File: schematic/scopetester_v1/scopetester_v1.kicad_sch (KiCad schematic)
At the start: 42 parts, among them J1 CON_PWR, J2 Conn_01x04, J3 AVR_ISP, SW1 SW_Push, U1 ATmega8A-P, Y1 12MHz

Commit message: Multiple fixes to PCB layout (not final)
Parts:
- added JP1: Jumper_2_Bridged, Resistor_THT:R_Axial_DIN0207_L6.3mm_D2.5mm_P7.62mm_Horizontal, symbol Jumper:Jumper_2_Bridged
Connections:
- net GND: now also JP1.1 (A), JP1.2 (B)
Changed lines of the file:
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@@
-    (stroke (width 0) (type default) (color 0 0 0 0))
-  )
-  (wire (pts (xy 255.27 58.42) (xy 257.81 58.42))
     (stroke (width 0) (type default) (color 0 0 0 0))
   )
@@
     (stroke (width 0) (type default) (color 0 0 0 0))
   )
+  (wire (pts (xy 255.27 60.96) (xy 257.81 60.96))
+    (stroke (width 0) (type default) (color 0 0 0 0))
+  )
   (wire (pts (xy 114.3 74.295) (xy 114.3 75.565))
     (stroke (width 0) (type default) (color 0 0 0 0))
@@
   )
   (wire (pts (xy 188.595 73.66) (xy 190.5 73.66))
-    (stroke (width 0) (type default) (color 0 0 0 0))
-  )
-  (wire (pts (xy 255.27 60.96) (xy 257.81 60.96))
     (stroke (width 0) (type default) (color 0 0 0 0))
   )
@@
   )
   (wire (pts (xy 129.54 122.555) (xy 133.35 122.555))
+    (stroke (width 0) (type default) (color 0 0 0 0))
+  )
+  (wire (pts (xy 255.27 58.42) (xy 257.81 58.42))
     (stroke (width 0) (type default) (color 0 0 0 0))
   )
@@
     )
     (property "Datasheet" "~" (id 3) (at 201.295 63.5 0)
+      (effects (font (size 1.27 1.27)) hide)
+    )
+    (pin "1")
+    (pin "2")
+  )
+  (symbol (lib_id "Jumper:Jumper_2_Bridged") (at 32.385 45.72 0) (unit 1)
+    (in_bom yes) (on_board yes) (fields_autoplaced)
+    (property "Reference" "JP1" (id 0) (at 32.385 39.37 0))
+    (property "Value" "Jumper_2_Bridged" (id 1) (at 32.385 41.91 0))
+    (property "Footprint" "Resistor_THT:R_Axial_DIN0207_L6.3mm_D2.5mm_P7.62mm_Horizontal" (id 2) (at 32.385 45.72 0)
+      (effects (font (size 1.27 1.27)) hide)
+    )
+    (property "Datasheet" "~" (id 3) (at 32.385 45.72 0)
       (effects (font (size 1.27 1.27)) hide)
     )
@@
     (pin "1")
   )
+  (symbol (lib_id "power:GND") (at 27.305 45.72 270) (unit 1)
+    (in_bom yes) (on_board yes)
+    (property "Reference" "#PWR0117" (id 0) (at 20.955 45.72 0)
+      (effects (font (size 1.27 1.27)) hide)
+    )
+    (property "Value" "GND" (id 1) (at 23.495 48.26 90)
+      (effects (font (size 1.27 1.27)) (justify left))
+    )
+    (property "Footprint" "" (id 2) (at 27.305 45.72 0)
+      (effects (font (size 1.27 1.27)) hide)
+    )
+    (property "Datasheet" "" (id 3) (at 27.305 45.72 0)
+      (effects (font (size 1.27 1.27)) hide)
+    )
+    (pin "1")
+  )
   (symbol (lib_id "Device:LED_Small") (at 190.5 140.335 180) (unit 1)
     (in_bom yes) (on_board yes)
@@
     (pin "1")
     (pin "2")
+  )
+  (symbol (lib_id "power:GND") (at 37.465 45.72 90) (unit 1)
+    (in_bom yes) (on_board yes)
+    (property "Reference" "#PWR0118" (id 0) (at 43.815 45.72 0)
+      (effects (font (size 1.27 1.27)) hide)
+    )
+    (property "Value" "GND" (id 1) (at 37.465 48.26 90)
+      (effects (font (size 1.27 1.27)) (justify right))
+    )
+    (property "Footprint" "" (id 2) (at 37.465 45.72 0)
+      (effects (font (size 1.27 1.27)) hide)
+    )
+    (property "Datasheet" "" (id 3) (at 37.465 45.72 0)
+      (effects (font (size 1.27 1.27)) hide)
+    )
+    (pin "1")
   )
   (symbol (lib_id "power:PWR_FLAG") (at 33.655 60.96 0) (unit 1)
@@
       (reference "#PWR0116") (unit 1) (value "+5V") (footprint "")
     )
+    (path "/c994bb30-108d-4af6-8371-cb0f6e510171"
+      (reference "#PWR0117") (unit 1) (value "GND") (footprint "")
+    )
+    (path "/f6663217-147d-4ee7-86df-cf836d7ea2b6"
+      (reference "#PWR0118") (unit 1) (value "GND") (footprint "")
+    )
     (path "/d296a615-c4ba-40da-b84d-31d01d3ec12b"
       (reference "C1") (unit 1) (value "100nF") (footprint "Capacitor_THT:C_Disc_D3.0mm_W1.6mm_P2.50mm")
@@
       (reference "J3") (unit 1) (value "AVR_ISP") (footprint "Connector_PinHeader_2.54mm:PinHeader_2x05_P2.54mm_Vertical")
     )
+    (path "/12dfce3d-9007-49ac-a6a4-dff735485df5"
+      (reference "JP1") (unit 1) (value "Jumper_2_Bridged") (footprint "Resistor_THT:R_Axial_DIN0207_L6.3mm_D2.5mm_P7.62mm_Horizontal")
+    )
     (path "/b4a94ed3-be86-4149-a3b1-4521ed9fb34c"

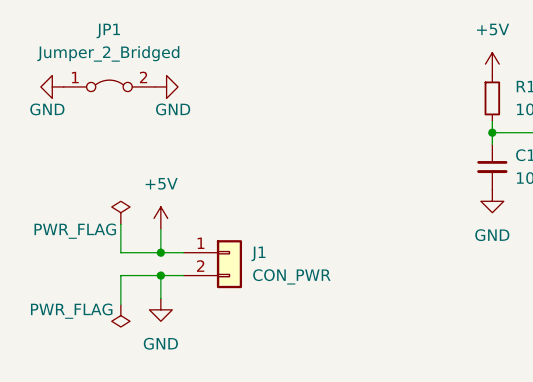
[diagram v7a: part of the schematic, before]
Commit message: More compact PCB layout
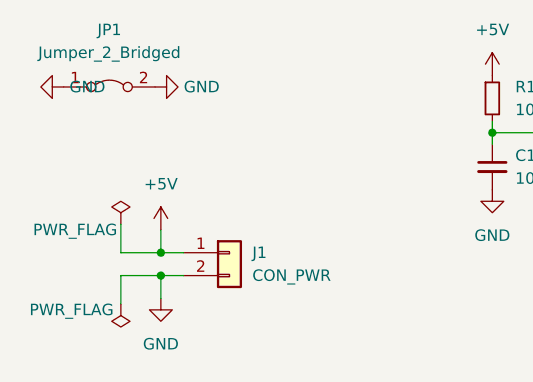
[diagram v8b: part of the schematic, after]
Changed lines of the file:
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@@
+    (pin "1")
+  )
+  (symbol (lib_id "power:GND") (at 27.305 45.72 270) (unit 1)
+    (in_bom yes) (on_board yes) (fields_autoplaced)
+    (property "Reference" "#PWR?" (id 0) (at 20.955 45.72 0)
+      (effects (font (size 1.27 1.27)) hide)
+    )
+    (property "Value" "GND" (id 1) (at 27.94 45.7199 90)
+      (effects (font (size 1.27 1.27)) (justify left))
+    )
+    (property "Footprint" "" (id 2) (at 27.305 45.72 0)
+      (effects (font (size 1.27 1.27)) hide)
+    )
+    (property "Datasheet" "" (id 3) (at 27.305 45.72 0)
+      (effects (font (size 1.27 1.27)) hide)
+    )
     (pin "1")
   )
@@
     (pin "1")
     (pin "2")
+  )
+  (symbol (lib_id "power:GND") (at 37.465 45.72 90) (unit 1)
+    (in_bom yes) (on_board yes) (fields_autoplaced)
+    (property "Reference" "#PWR?" (id 0) (at 43.815 45.72 0)
+      (effects (font (size 1.27 1.27)) hide)
+    )
+    (property "Value" "GND" (id 1) (at 40.64 45.7199 90)
+      (effects (font (size 1.27 1.27)) (justify right))
+    )
+    (property "Footprint" "" (id 2) (at 37.465 45.72 0)
+      (effects (font (size 1.27 1.27)) hide)
+    )
+    (property "Datasheet" "" (id 3) (at 37.465 45.72 0)
+      (effects (font (size 1.27 1.27)) hide)
+    )
+    (pin "1")
   )
   (symbol (lib_id "power:+5V") (at 135.89 46.99 0) (unit 1)
@@
     (pin "1")
   )
-  (symbol (lib_id "power:GND") (at 27.305 45.72 270) (unit 1)
-    (in_bom yes) (on_board yes)
-    (property "Reference" "#PWR0117" (id 0) (at 20.955 45.72 0)
-      (effects (font (size 1.27 1.27)) hide)
-    )
-    (property "Value" "GND" (id 1) (at 23.495 48.26 90)
-      (effects (font (size 1.27 1.27)) (justify left))
-    )
-    (property "Footprint" "" (id 2) (at 27.305 45.72 0)
-      (effects (font (size 1.27 1.27)) hide)
-    )
-    (property "Datasheet" "" (id 3) (at 27.305 45.72 0)
-      (effects (font (size 1.27 1.27)) hide)
-    )
-    (pin "1")
-  )
   (symbol (lib_id "Device:LED_Small") (at 190.5 140.335 180) (unit 1)
     (in_bom yes) (on_board yes)
@@
     (pin "1")
     (pin "2")
-  )
-  (symbol (lib_id "power:GND") (at 37.465 45.72 90) (unit 1)
-    (in_bom yes) (on_board yes)
-    (property "Reference" "#PWR0118" (id 0) (at 43.815 45.72 0)
-      (effects (font (size 1.27 1.27)) hide)
-    )
-    (property "Value" "GND" (id 1) (at 37.465 48.26 90)
-      (effects (font (size 1.27 1.27)) (justify right))
-    )
-    (property "Footprint" "" (id 2) (at 37.465 45.72 0)
-      (effects (font (size 1.27 1.27)) hide)
-    )
-    (property "Datasheet" "" (id 3) (at 37.465 45.72 0)
-      (effects (font (size 1.27 1.27)) hide)
-    )
-    (pin "1")
   )
   (symbol (lib_id "power:PWR_FLAG") (at 33.655 60.96 0) (unit 1)
@@
       (reference "#PWR0116") (unit 1) (value "+5V") (footprint "")
     )
-    (path "/c994bb30-108d-4af6-8371-cb0f6e510171"
-      (reference "#PWR0117") (unit 1) (value "GND") (footprint "")
-    )
-    (path "/f6663217-147d-4ee7-86df-cf836d7ea2b6"
-      (reference "#PWR0118") (unit 1) (value "GND") (footprint "")
+    (path "/43b02ddd-f584-4f99-ba88-aa75ee88b79d"
+      (reference "#PWR?") (unit 1) (value "GND") (footprint "")
+    )
+    (path "/49d74109-df68-473a-922a-f2d20aa21baf"
+      (reference "#PWR?") (unit 1) (value "GND") (footprint "")
     )
     (path "/d296a615-c4ba-40da-b84d-31d01d3ec12b"
